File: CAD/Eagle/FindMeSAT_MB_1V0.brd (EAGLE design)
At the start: 99 x 49.2 mm, 131 parts, among them J291 MCX-J-P-X-RA-SM1, J685 SMA_CON, J701 MOLEX_105017-0001, J801 MICROSIM-8P_SDCARD-8P_MOLEX-1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, J901 JST_S3B-XH-A, Q101 ABS07-32.768KHZ, Q651 ABM3B-16MHZ-10-R50-1-U, U1001 CFPT-141-20MHZ, U101 ATXMEGA256A3BU-AU, U1011 OPA354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

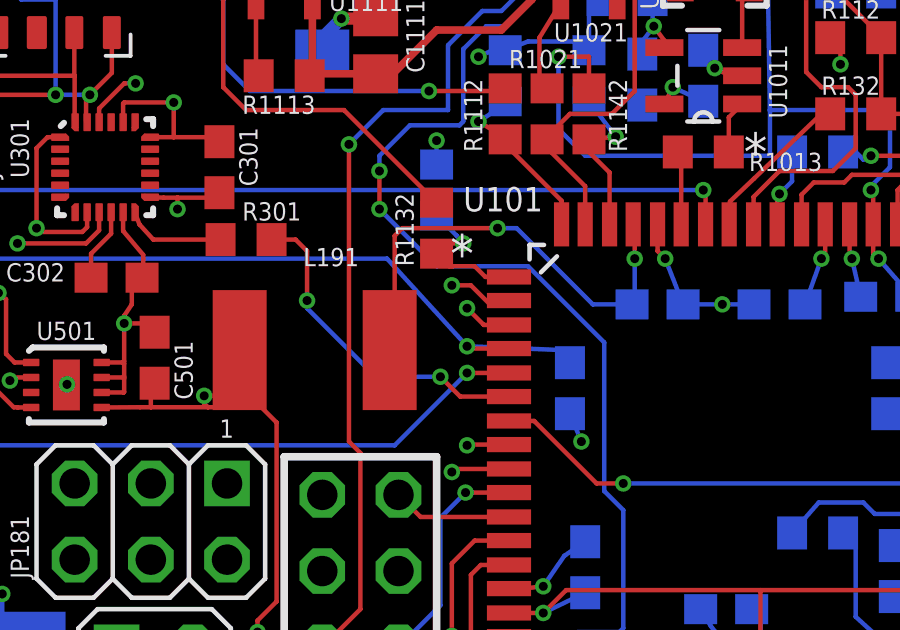
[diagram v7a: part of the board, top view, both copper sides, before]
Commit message: Eagle - replaced 10uH device by a 0603 package, optional Gfx-LCD added to the Docs
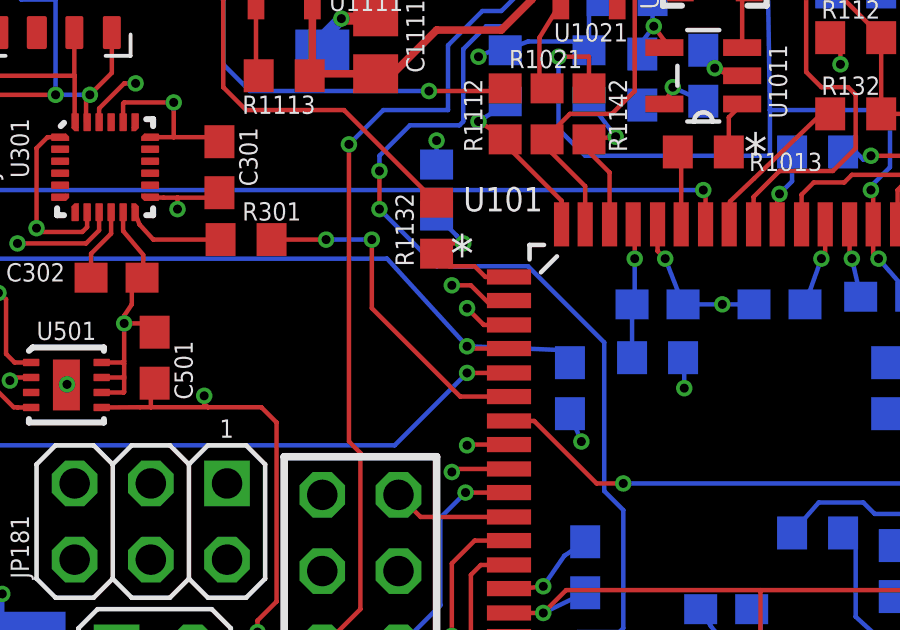
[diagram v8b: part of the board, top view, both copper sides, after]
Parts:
- L191: device rcl:L5650M -> rcl:R0603
- moved L191 11.4 mm to (68.3, 18.5), flipped to the bottom
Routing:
- net AVCC: track 15.8 -> 4.58 mm, vias 2 -> 1
- net +3V3: track 103.1 -> 100.3 mm, vias 18 -> 19
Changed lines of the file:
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@@
 <attribute name="VALUE" x="66.5988" y="14.9098" size="0.6096" layer="27" ratio="10" rot="SR0"/>
 </element>
-<element name="L191" library="rcl" package="L5650M" value="10uH" x="56.896" y="18.796" smashed="yes" rot="R180">
-<attribute name="NAME" x="56.515" y="21.59" size="0.6096" layer="25"/>
-<attribute name="VALUE" x="57.531" y="17.653" size="0.6096" layer="27" rot="R90"/>
+<element name="L191" library="rcl" package="R0603" value="10uH" x="68.326" y="18.542" smashed="yes" rot="MR180">
+<attribute name="NAME" x="71.882" y="18.034" size="0.6096" layer="26" rot="MR0"/>
+<attribute name="VALUE" x="67.437" y="18.923" size="0.6096" layer="28" rot="MR180"/>
 </element>
 <element name="C191" library="rcl" package="C0603" value="100nF" x="65.913" y="11.557" smashed="yes" rot="MR90">
@@
 </element>
 <element name="C196" library="rcl" package="C0603" value="100nF" x="68.326" y="20.32" smashed="yes" rot="MR180">
-<attribute name="NAME" x="69.977" y="18.796" size="0.6096" layer="26" rot="MR0"/>
+<attribute name="NAME" x="67.31" y="20.955" size="0.6096" layer="26" rot="MR0"/>
 <attribute name="VALUE" x="68.834" y="19.939" size="0.6096" layer="28" rot="MR0"/>
 </element>
@@
 <contactref element="JP201" pad="1"/>
 <wire x1="44.196" y1="32.893" x2="44.196" y2="27.813" width="0.4064" layer="16"/>
-<wire x1="83.898" y1="37.26" x2="83.82" y2="37.26" width="0" layer="19" extent="16-16"/>
 <wire x1="43.942" y1="20.828" x2="43.18" y2="21.59" width="0.15" layer="16"/>
 <wire x1="43.18" y1="21.59" x2="43.18" y2="22.225" width="0.15" layer="16"/>
@@
 <wire x1="43.053" y1="23.114" x2="43.053" y2="26.67" width="0.15" layer="1"/>
 <wire x1="43.053" y1="26.67" x2="44.196" y2="27.813" width="0.15" layer="1"/>
+<wire x1="83.898" y1="37.26" x2="83.82" y2="37.26" width="0" layer="19" extent="16-16"/>
 </signal>
 <signal name="SW">
@@
 <wire x1="49.149" y1="22.733" x2="47.752" y2="22.733" width="0.15" layer="1"/>
 <wire x1="47.752" y1="22.733" x2="47.625" y2="22.86" width="0.15" layer="1"/>
-<wire x1="54.396" y1="18.796" x2="53.721" y2="19.725" width="0.15" layer="1"/>
 <contactref element="C501" pad="1"/>
 <contactref element="U501" pad="5"/>
@@
 <wire x1="51.074" y1="16.891" x2="51.435" y2="16.891" width="0.15" layer="1"/>
 <wire x1="51.435" y1="16.891" x2="53.34" y2="16.891" width="0.15" layer="1"/>
-<wire x1="53.34" y1="16.891" x2="53.721" y2="16.891" width="0.15" layer="1"/>
 <wire x1="51.562" y1="17.692" x2="51.435" y2="17.565" width="0.15" layer="1"/>
 <wire x1="51.435" y1="17.565" x2="51.435" y2="16.891" width="0.15" layer="1"/>
@@
 <wire x1="53.213" y1="17.272" x2="53.213" y2="17.018" width="0.15" layer="1"/>
 <wire x1="53.213" y1="17.018" x2="53.34" y2="16.891" width="0.15" layer="1"/>
-<wire x1="53.213" y1="17.272" x2="54.396" y2="17.272" width="0.15" layer="1"/>
-<wire x1="54.396" y1="17.272" x2="54.396" y2="18.796" width="0.15" layer="1"/>
 <wire x1="77.724" y1="10.795" x2="71.755" y2="10.795" width="0.15" layer="1"/>
 <wire x1="71.755" y1="10.795" x2="71.755" y2="8.636" width="0.15" layer="1"/>
@@
 <wire x1="54.991" y1="9.779" x2="54.991" y2="9.398" width="0.15" layer="1"/>
 <wire x1="55.118" y1="16.891" x2="54.396" y2="16.891" width="0.15" layer="1"/>
-<wire x1="54.396" y1="16.891" x2="54.396" y2="17.272" width="0.15" layer="1"/>
 <via x="54.991" y="9.398" extent="1-16" drill="0.3" shape="octagon"/>
 <wire x1="54.991" y1="9.398" x2="54.991" y2="8.509" width="0.15" layer="16"/>
@@
 <via x="52.324" y="23.495" extent="1-16" drill="0.3" shape="octagon"/>
 <wire x1="52.324" y1="23.495" x2="52.324" y2="23.876" width="0.15" layer="1"/>
+<via x="69.215" y="17.526" extent="1-16" drill="0.3" shape="octagon"/>
+<wire x1="69.215" y1="17.526" x2="69.215" y2="18.288" width="0.15" layer="16"/>
+<wire x1="53.34" y1="16.891" x2="54.356" y2="16.891" width="0.15" layer="1"/>
 <wire x1="74.422" y1="28.868" x2="81.28" y2="31.75" width="0" layer="19" extent="1-1"/>
 <wire x1="69.85" y1="27.09" x2="74.08" y2="29.21" width="0" layer="19" extent="1-16"/>
@@
 <wire x1="73.914" y1="22.987" x2="74.422" y2="28.321" width="0" layer="19" extent="1-1"/>
 <wire x1="75.946" y1="18.376" x2="73.24" y2="20.32" width="0" layer="19" extent="16-16"/>
+<wire x1="69.176" y1="18.542" x2="73.24" y2="20.32" width="0" layer="19" extent="16-16"/>
+<wire x1="69.215" y1="18.288" x2="69.176" y2="18.542" width="0" layer="19" extent="16-16"/>
 <wire x1="61.126" y1="33.02" x2="66.714" y2="33.02" width="0" layer="19" extent="16-16"/>
 <wire x1="76.2" y1="12.28" x2="75.946" y2="18.376" width="0" layer="19" extent="16-16"/>
 <wire x1="59.69" y1="11.43" x2="63.373" y2="10.033" width="0" layer="19" extent="1-1"/>
 <wire x1="55.626" y1="10.414" x2="59.69" y2="11.43" width="0" layer="19" extent="1-1"/>
-<wire x1="52.324" y1="23.495" x2="53.721" y2="19.725" width="0" layer="19" extent="1-1"/>
-<wire x1="49.311" y1="23.392" x2="51.4635" y2="23.892" width="0" layer="19" extent="1-1"/>
+<wire x1="54.356" y1="16.891" x2="54.396" y2="16.891" width="0" layer="19" extent="1-1"/>
+<wire x1="49.149" y1="22.733" x2="51.562" y2="17.692" width="0" layer="19" extent="1-1"/>
 <wire x1="49.711" y1="26.392" x2="48.3585" y2="25.892" width="0" layer="19" extent="1-1"/>
+<wire x1="51.4635" y1="23.892" x2="49.311" y2="23.392" width="0" layer="19" extent="1-1"/>
 <wire x1="50.135" y1="31.58" x2="50.546" y2="27.686" width="0" layer="19" extent="1-1"/>
 <wire x1="50.292" y1="3.81" x2="55.118" y2="8.062" width="0" layer="19" extent="16-16"/>
@@
 <wire x1="67.5132" y1="22.987" x2="67.564" y2="22.987" width="0.15" layer="1"/>
 <wire x1="67.564" y1="22.987" x2="67.564" y2="21.844" width="0.15" layer="1"/>
-<wire x1="67.476" y1="20.32" x2="66.167" y2="20.32" width="0.15" layer="16"/>
-<wire x1="66.167" y1="20.32" x2="63.627" y2="22.86" width="0.15" layer="16"/>
-<wire x1="63.627" y1="22.86" x2="62.992" y2="22.86" width="0.15" layer="16"/>
-<wire x1="59.396" y1="18.796" x2="59.563" y2="18.883" width="0.15" layer="1"/>
-<wire x1="59.563" y1="18.883" x2="59.563" y2="22.606" width="0.15" layer="1"/>
-<wire x1="59.563" y1="22.606" x2="59.817" y2="22.86" width="0.15" layer="1"/>
-<via x="62.992" y="22.86" extent="1-16" drill="0.3" shape="octagon"/>
-<wire x1="59.817" y1="22.86" x2="62.992" y2="22.86" width="0.15" layer="1"/>
+<wire x1="67.476" y1="18.542" x2="67.476" y2="20.32" width="0.15" layer="16"/>
 </signal>
 <signal name="+3V0">
@@
 <contactref element="U101" pad="6"/>
 <wire x1="63.373" y1="17.2466" x2="61.7474" y2="17.2466" width="0.15" layer="1"/>
-<wire x1="61.7474" y1="17.2466" x2="61.087" y2="17.907" width="0.15" layer="1"/>
-<via x="61.087" y="17.907" extent="1-16" drill="0.3" shape="octagon"/>
 <contactref element="R301" pad="2"/>
-<wire x1="55.46" y1="22.479" x2="56.261" y2="22.479" width="0.15" layer="1"/>
-<wire x1="56.261" y1="22.479" x2="56.642" y2="22.098" width="0.15" layer="1"/>
-<wire x1="56.642" y1="22.098" x2="56.642" y2="20.447" width="0.15" layer="1"/>
-<via x="56.642" y="20.447" extent="1-16" drill="0.3" shape="octagon"/>
-<wire x1="56.642" y1="20.447" x2="56.642" y2="20.193" width="0.15" layer="16"/>
-<wire x1="56.642" y1="20.193" x2="58.928" y2="17.907" width="0.15" layer="16"/>
-<wire x1="58.928" y1="17.907" x2="61.087" y2="17.907" width="0.15" layer="16"/>
+<wire x1="61.7474" y1="17.2466" x2="58.801" y2="20.193" width="0.15" layer="1"/>
+<wire x1="58.801" y1="20.193" x2="58.801" y2="22.479" width="0.15" layer="1"/>
+<via x="58.801" y="22.479" extent="1-16" drill="0.3" shape="octagon"/>
+<wire x1="58.801" y1="22.479" x2="57.277" y2="22.479" width="0.15" layer="16"/>
+<via x="57.277" y="22.479" extent="1-16" drill="0.3" shape="octagon"/>
+<wire x1="57.277" y1="22.479" x2="55.753" y2="22.479" width="0.15" layer="1"/>
+<wire x1="55.753" y1="22.479" x2="55.46" y2="22.479" width="0.15" layer="1"/>
 </signal>
 <signal name="GAM_RO">
